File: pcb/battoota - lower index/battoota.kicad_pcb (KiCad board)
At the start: 2 copper layers, 128.3 x 99.3 mm, 38 parts

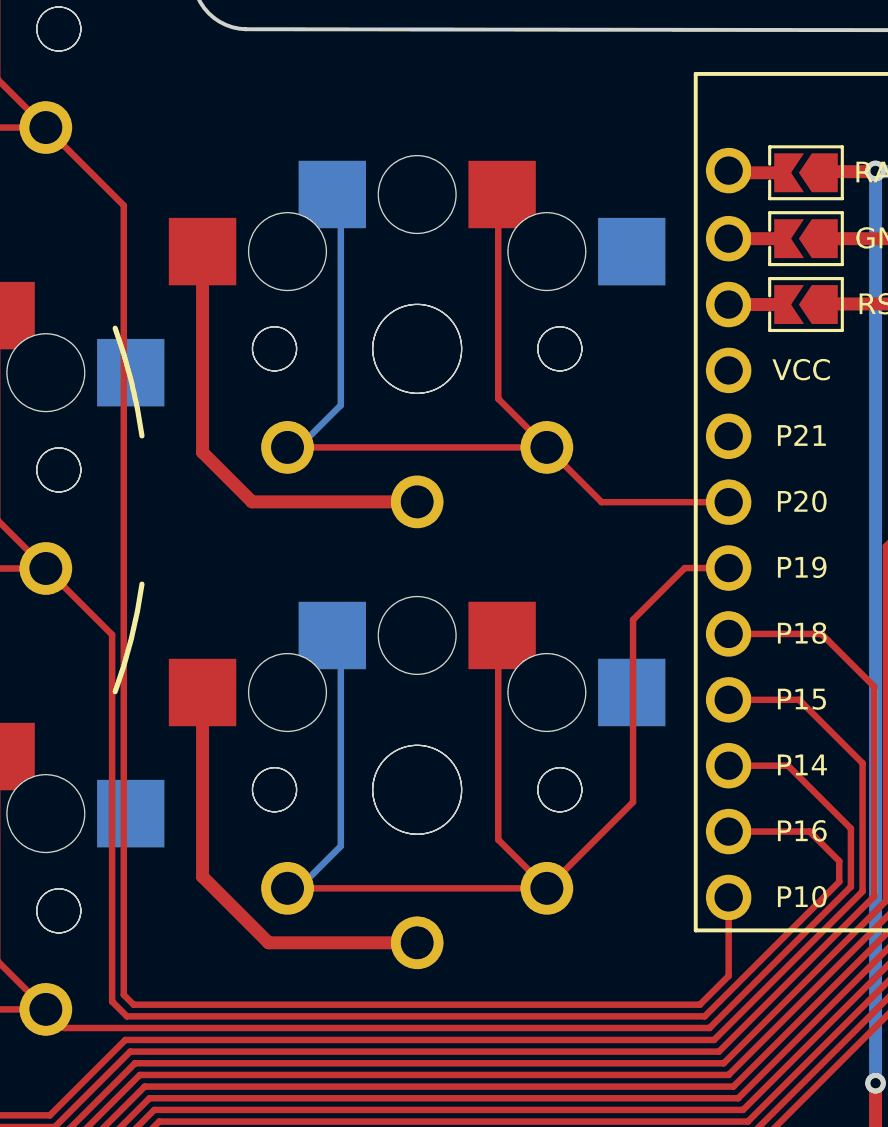
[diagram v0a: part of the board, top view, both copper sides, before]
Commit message: remove curvy and make inner index closer
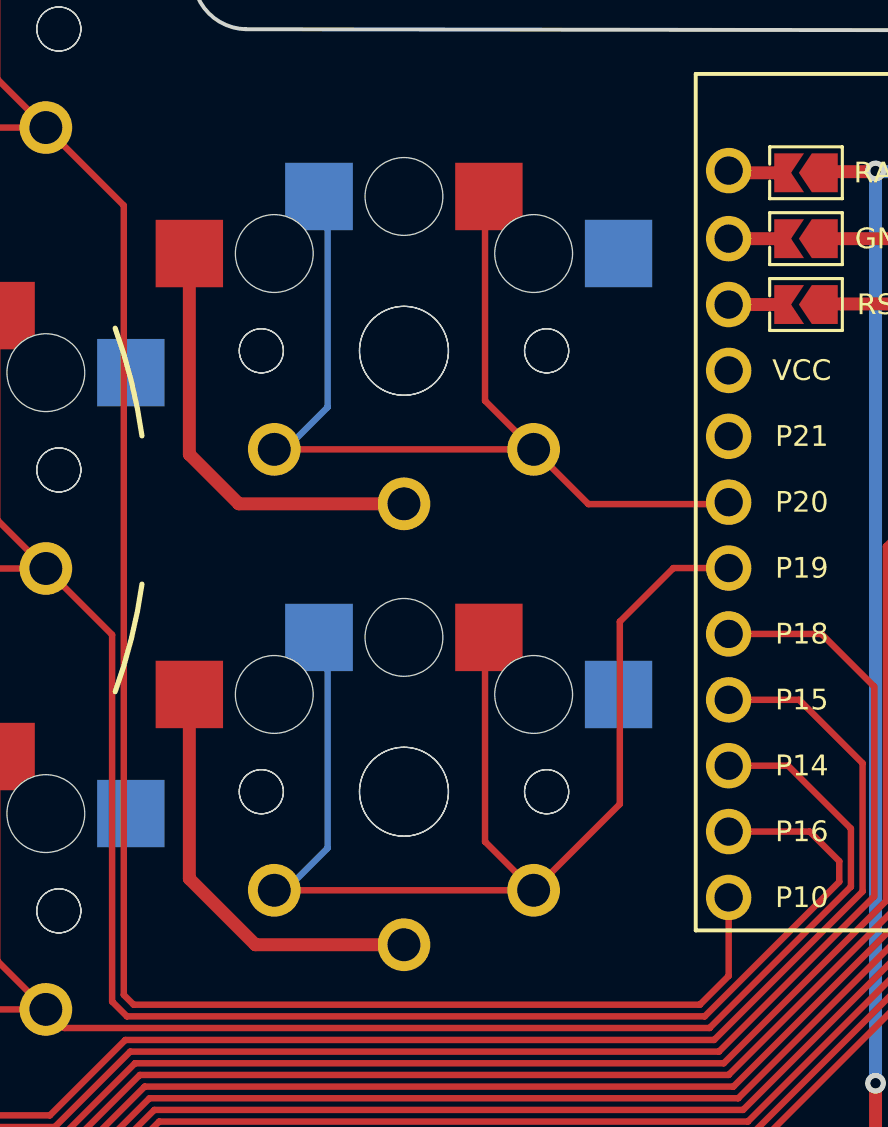
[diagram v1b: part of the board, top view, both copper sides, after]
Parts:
- moved S27 0.52 mm to (134.2, -77.3)
- moved S28 0.52 mm to (134.2, -77.3)
- moved S29 0.52 mm to (134.2, -94.3)
- moved S30 0.52 mm to (134.2, -94.3)
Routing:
- net P19: track 47.7 -> 48.2 mm
- net P20: track 38.9 -> 39.5 mm
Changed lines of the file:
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@@
   )
   (footprint "PG1350" (layer "F.Cu")
-    (at 134.728078 -77.354137 180)
+    (at 134.21828 -77.278852 180)
     (attr through_hole)
     (fp_text reference "S28" (at 0 0) (layer "F.SilkS") hide
@@
   )
   (footprint "PG1350" (layer "F.Cu")
-    (at 134.728078 -94.354137)
+    (at 134.21828 -94.278852)
     (attr through_hole)
     (fp_text reference "S29" (at 0 0) (layer "F.SilkS") hide
@@
   )
   (footprint "PG1350" (layer "F.Cu")
-    (at 134.728078 -77.354137)
+    (at 134.21828 -77.278852)
     (attr through_hole)
     (fp_text reference "S27" (at 0 0) (layer "F.SilkS") hide
@@
   )
   (footprint "PG1350" (layer "F.Cu")
-    (at 134.728078 -94.354137 180)
+    (at 134.21828 -94.278852 180)
     (attr through_hole)
     (fp_text reference "S30" (at 0 0) (layer "F.SilkS") hide
@@
   (segment (start 63.384822 -105.421809) (end 62.586645 -106.219986) (width 0.5) (layer "F.Cu") (net 2))
   (segment (start 96.21751 -74.301308) (end 89.760656 -74.301308) (width 0.5) (layer "F.Cu") (net 2))
-  (segment (start 134.728078 -88.454137) (end 128.361699 -88.454137) (width 0.5) (layer "F.Cu") (net 2))
+  (segment (start 134.21828 -88.378852) (end 127.851901 -88.378852) (width 0.5) (layer "F.Cu") (net 2))
   (segment (start 63.384822 -100.80225) (end 63.384822 -105.421809) (width 0.5) (layer "F.Cu") (net 2))
-  (segment (start 129.000596 -71.454137) (end 126.453078 -74.001655) (width 0.5) (layer "F.Cu") (net 2))
+  (segment (start 128.490798 -71.378852) (end 125.94328 -73.92637) (width 0.5) (layer "F.Cu") (net 2))
   (segment (start 75.363653 -82.192969) (end 74.347654 -81.17697) (width 0.5) (layer "F.Cu") (net 2))
   (segment (start 115.411087 -66.786017) (end 109.81576 -66.786017) (width 0.5) (layer "F.Cu") (net 2))
-  (segment (start 126.453078 -90.362758) (end 126.453078 -98.104137) (width 0.5) (layer "F.Cu") (net 2))
+  (segment (start 125.94328 -90.287473) (end 125.94328 -98.028852) (width 0.5) (layer "F.Cu") (net 2))
   (segment (start 108.15356 -68.448217) (end 108.15356 -75.418544) (width 0.5) (layer "F.Cu") (net 2))
   (segment (start 62.586645 -106.219986) (end 62.586645 -107.001157) (width 0.5) (layer "F.Cu") (net 2))
@@
   (segment (start 132.364014 -43.339776) (end 127.939105 -43.339776) (width 0.5) (layer "F.Cu") (net 2))
   (segment (start 53.137791 -59.489222) (end 49.917361 -62.709652) (width 0.5) (layer "F.Cu") (net 2))
-  (segment (start 134.728078 -71.454137) (end 129.000596 -71.454137) (width 0.5) (layer "F.Cu") (net 2))
+  (segment (start 134.21828 -71.378852) (end 128.490798 -71.378852) (width 0.5) (layer "F.Cu") (net 2))
   (segment (start 107.136087 -103.216201) (end 107.136087 -110.436017) (width 0.5) (layer "F.Cu") (net 2))
   (segment (start 86.601289 -108.171928) (end 86.570217 -108.140856) (width 0.5) (layer "F.Cu") (net 2))
@@
   (segment (start 108.973745 -83.786017) (end 107.136087 -85.623675) (width 0.5) (layer "F.Cu") (net 2))
   (segment (start 154.304587 -98.650426) (end 154.256703 -98.602542) (width 0.5) (layer "F.Cu") (net 2))
-  (segment (start 128.361699 -88.454137) (end 126.453078 -90.362758) (width 0.5) (layer "F.Cu") (net 2))
+  (segment (start 127.851901 -88.378852) (end 125.94328 -90.287473) (width 0.5) (layer "F.Cu") (net 2))
   (segment (start 44.864298 -78.586881) (end 44.864298 -82.864875) (width 0.5) (layer "F.Cu") (net 2))
   (segment (start 86.570217 -108.140856) (end 84.169651 -110.541422) (width 0.5) (layer "F.Cu") (net 2))
@@
   (segment (start 44.864298 -82.864875) (end 43.832443 -83.89673) (width 0.5) (layer "F.Cu") (net 2))
   (segment (start 49.917361 -62.709652) (end 49.917361 -65.987885) (width 0.5) (layer "F.Cu") (net 2))
-  (segment (start 126.453078 -74.001655) (end 126.453078 -81.104137) (width 0.5) (layer "F.Cu") (net 2))
+  (segment (start 125.94328 -73.92637) (end 125.94328 -81.028852) (width 0.5) (layer "F.Cu") (net 2))
   (segment (start 84.169651 -110.541422) (end 84.169651 -117.063993) (width 0.5) (layer "F.Cu") (net 2))
   (via (at 154.304587 -98.650426) (size 0.8) (drill 0.4) (layers "F.Cu" "B.Cu") (free) (net 2))
@@
   (segment (start 112.285608 -104.760538) (end 110.411087 -102.886017) (width 0.25) (layer "B.Cu") (net 11))
   (segment (start 112.285608 -113.029475) (end 112.285608 -104.760538) (width 0.25) (layer "B.Cu") (net 11))
-  (segment (start 137.853557 -75.428658) (end 137.853557 -83.154616) (width 0.25) (layer "F.Cu") (net 12))
-  (segment (start 139.728078 -73.554137) (end 137.853557 -75.428658) (width 0.25) (layer "F.Cu") (net 12))
-  (segment (start 137.853557 -83.154616) (end 138.003078 -83.304137) (width 0.25) (layer "F.Cu") (net 12))
-  (segment (start 143.050689 -83.90926) (end 145.043971 -85.902542) (width 0.25) (layer "F.Cu") (net 12))
-  (segment (start 139.728078 -73.554137) (end 143.050689 -76.876748) (width 0.25) (layer "F.Cu") (net 12))
-  (segment (start 143.050689 -76.876748) (end 143.050689 -83.90926) (width 0.25) (layer "F.Cu") (net 12))
-  (segment (start 145.043971 -85.902542) (end 146.737213 -85.902542) (width 0.25) (layer "F.Cu") (net 12))
-  (segment (start 129.728078 -73.554137) (end 139.728078 -73.554137) (width 0.25) (layer "F.Cu") (net 12))
-  (segment (start 131.782744 -75.177393) (end 129.588503 -72.983152) (width 0.25) (layer "B.Cu") (net 12))
-  (segment (start 131.782744 -82.263911) (end 131.782744 -75.177393) (width 0.25) (layer "B.Cu") (net 12))
-  (segment (start 131.313503 -82.733152) (end 131.782744 -82.263911) (width 0.25) (layer "B.Cu") (net 12))
-  (segment (start 141.839673 -88.442542) (end 146.737213 -88.442542) (width 0.25) (layer "F.Cu") (net 13))
-  (segment (start 137.853557 -92.428658) (end 137.853557 -100.154616) (width 0.25) (layer "F.Cu") (net 13))
-  (segment (start 137.853557 -100.154616) (end 138.003078 -100.304137) (width 0.25) (layer "F.Cu") (net 13))
-  (segment (start 139.728078 -90.554137) (end 137.853557 -92.428658) (width 0.25) (layer "F.Cu") (net 13))
-  (segment (start 139.728078 -90.554137) (end 141.839673 -88.442542) (width 0.25) (layer "F.Cu") (net 13))
-  (segment (start 129.728078 -90.554137) (end 139.728078 -90.554137) (width 0.25) (layer "F.Cu") (net 13))
-  (segment (start 131.782744 -99.263911) (end 131.782744 -92.177393) (width 0.25) (layer "B.Cu") (net 13))
-  (segment (start 130.159488 -90.554137) (end 129.728078 -90.554137) (width 0.25) (layer "B.Cu") (net 13))
-  (segment (start 131.782744 -92.177393) (end 130.159488 -90.554137) (width 0.25) (layer "B.Cu") (net 13))
-  (segment (start 131.313503 -99.733152) (end 131.782744 -99.263911) (width 0.25) (layer "B.Cu") (net 13))
+  (segment (start 144.607863 -85.902542) (end 146.737213 -85.902542) (width 0.25) (layer "F.Cu") (net 12))
+  (segment (start 137.343759 -75.353373) (end 137.343759 -83.079331) (width 0.25) (layer "F.Cu") (net 12))
+  (segment (start 142.540891 -83.83557) (end 144.607863 -85.902542) (width 0.25) (layer "F.Cu") (net 12))
+  (segment (start 142.540891 -76.801463) (end 142.540891 -83.83557) (width 0.25) (layer "F.Cu") (net 12))
+  (segment (start 139.21828 -73.478852) (end 137.343759 -75.353373) (width 0.25) (layer "F.Cu") (net 12))
+  (segment (start 137.343759 -83.079331) (end 137.49328 -83.228852) (width 0.25) (layer "F.Cu") (net 12))
+  (segment (start 139.21828 -73.478852) (end 142.540891 -76.801463) (width 0.25) (layer "F.Cu") (net 12))
+  (segment (start 129.21828 -73.478852) (end 139.21828 -73.478852) (width 0.25) (layer "F.Cu") (net 12))
+  (segment (start 131.272946 -75.102108) (end 129.078705 -72.907867) (width 0.25) (layer "B.Cu") (net 12))
+  (segment (start 131.272946 -82.188626) (end 131.272946 -75.102108) (width 0.25) (layer "B.Cu") (net 12))
+  (segment (start 130.803705 -82.657867) (end 131.272946 -82.188626) (width 0.25) (layer "B.Cu") (net 12))
+  (segment (start 141.329875 -88.367257) (end 146.661928 -88.367257) (width 0.25) (layer "F.Cu") (net 13))
+  (segment (start 139.21828 -90.478852) (end 141.329875 -88.367257) (width 0.25) (layer "F.Cu") (net 13))
+  (segment (start 137.343759 -92.353373) (end 137.343759 -100.079331) (width 0.25) (layer "F.Cu") (net 13))
+  (segment (start 137.343759 -100.079331) (end 137.49328 -100.228852) (width 0.25) (layer "F.Cu") (net 13))
+  (segment (start 139.21828 -90.478852) (end 137.343759 -92.353373) (width 0.25) (layer "F.Cu") (net 13))
+  (segment (start 146.661928 -88.367257) (end 146.737213 -88.442542) (width 0.25) (layer "F.Cu") (net 13))
+  (segment (start 129.21828 -90.478852) (end 139.21828 -90.478852) (width 0.25) (layer "F.Cu") (net 13))
+  (segment (start 131.272946 -99.188626) (end 131.272946 -92.102108) (width 0.25) (layer "B.Cu") (net 13))
+  (segment (start 129.64969 -90.478852) (end 129.21828 -90.478852) (width 0.25) (layer "B.Cu") (net 13))
+  (segment (start 131.272946 -92.102108) (end 129.64969 -90.478852) (width 0.25) (layer "B.Cu") (net 13))
+  (segment (start 130.803705 -99.657867) (end 131.272946 -99.188626) (width 0.25) (layer "B.Cu") (net 13))
   (segment (start 121.872336 -61.654585) (end 109.627476 -61.654585) (width 0.25) (layer "F.Cu") (net 15))
   (segment (start 93.841919 -71.588001) (end 89.748263 -71.588001) (width 0.25) (layer "F.Cu") (net 15))

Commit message: update battoota design
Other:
- board size 128.3 x 99.3 mm -> 124.7 x 97.3 mm
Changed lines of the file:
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@@
   (gr_line (start 126.088253 -108.703396) (end 125.984 -114.046) (layer "Edge.Cuts") (width 0.15))
   (gr_arc (start 82.233091 -118.259454) (mid 81.827408 -116.867619) (end 80.587997 -116.115527) (layer "Edge.Cuts") (width 0.15))
-  (gr_arc (start 167.528587 -47.330455) (mid 168.024672 -45.267049) (end 167.64 -43.18) (layer "Edge.Cuts") (width 0.15))
-  (gr_arc (start 167.528587 -47.330455) (mid 165.211835 -51.649611) (end 164.411087 -56.485027) (layer "Edge.Cuts") (width 0.15))
+  (gr_arc (start 164.439924 -43.880197) (mid 164.151212 -41.737454) (end 163.402658 -39.709063) (layer "Edge.Cuts") (width 0.15))
   (gr_line (start 60.120825 -110.475759) (end 61.630489 -101.874615) (layer "Edge.Cuts") (width 0.15))
   (gr_line (start 118.067797 -41.80264) (end 52.13573 -54.028933) (layer "Edge.Cuts") (width 0.15))
@@
   (gr_arc (start 128.117202 -106.676472) (mid 126.698658 -107.285463) (end 126.088253 -108.703396) (layer "Edge.Cuts") (width 0.15))
   (gr_arc (start 60.120826 -110.475759) (mid 60.452137 -111.970208) (end 61.743144 -112.792671) (layer "Edge.Cuts") (width 0.15))
-  (gr_line (start 156.354214 -25.985787) (end 167.64 -43.18) (layer "Edge.Cuts") (width 0.15))
+  (gr_line (start 157.334791 -28.728254) (end 163.402658 -39.709063) (layer "Edge.Cuts") (width 0.15))
   (gr_arc (start 118.067797 -41.80264) (mid 120.992158 -41.190657) (end 123.746692 -40.034594) (layer "Edge.Cuts") (width 0.15))
-  (gr_line (start 152.4 -25.4) (end 123.746692 -40.034594) (layer "Edge.Cuts") (width 0.15))
+  (gr_line (start 153.557891 -27.228602) (end 123.746692 -40.034594) (layer "Edge.Cuts") (width 0.15))
   (gr_arc (start 123.444 -116.84) (mid 125.278785 -115.956422) (end 125.984 -114.046) (layer "Edge.Cuts") (width 0.15))
-  (gr_arc (start 156.354214 -25.985787) (mid 154.473897 -25.039536) (end 152.4 -25.4) (layer "Edge.Cuts") (width 0.15))
+  (gr_arc (start 157.334791 -28.728254) (mid 155.731116 -27.261216) (end 153.557891 -27.228602) (layer "Edge.Cuts") (width 0.15))
   (gr_arc (start 39.815446 -88.161643) (mid 39.788585 -89.36909) (end 40.458272 -90.379598) (layer "Edge.Cuts") (width 0.15))
   (gr_line (start 102.139179 -122.500829) (end 102.517198 -118.831058) (layer "Edge.Cuts") (width 0.15))
@@
   (gr_line (start 82.23309 -118.259454) (end 82.016046 -120.740283) (layer "Edge.Cuts") (width 0.15))
   (gr_arc (start 162.411086 -106.629429) (mid 163.838502 -106.070136) (end 164.411086 -104.648) (layer "Edge.Cuts") (width 0.15))
-  (gr_line (start 164.411087 -56.485027) (end 164.411086 -104.648) (layer "Edge.Cuts") (width 0.15))
+  (gr_line (start 164.439924 -43.880197) (end 164.411086 -104.648) (layer "Edge.Cuts") (width 0.15))
   (segment (start 81.024544 -63.5) (end 71.12 -63.5) (width 0.25) (layer "F.Cu") (net 1))
   (segment (start 94.028116 -72.037521) (end 89.562066 -72.037521) (width 0.25) (layer "F.Cu") (net 1))

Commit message: pcb shape change
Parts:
- moved B1 0.66 mm to (163.2, -65.9)
- moved T1 0.26 mm to (162.5, -55.8)
- moved T2 0.26 mm to (162.5, -55.8)
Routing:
- net Braw: track 35.8 -> 37.0 mm
- net RST: track 38.3 -> 39.0 mm
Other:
- board size 124.7 x 97.3 mm -> 125.1 x 97.3 mm
